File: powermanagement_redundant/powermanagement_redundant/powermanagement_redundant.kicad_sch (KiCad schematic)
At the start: 48 parts, among them J1 Screw_Terminal_01x01, J2 Screw_Terminal_01x01, J3 Screw_Terminal_01x01, J4 Screw_Terminal_01x01, J5 Screw_Terminal_01x01, J6 Screw_Terminal_01x01, J7 Screw_Terminal_01x01, J8 Screw_Terminal_01x01, SW1 SW_DIP_x01, SW2 SW_DIP_x01

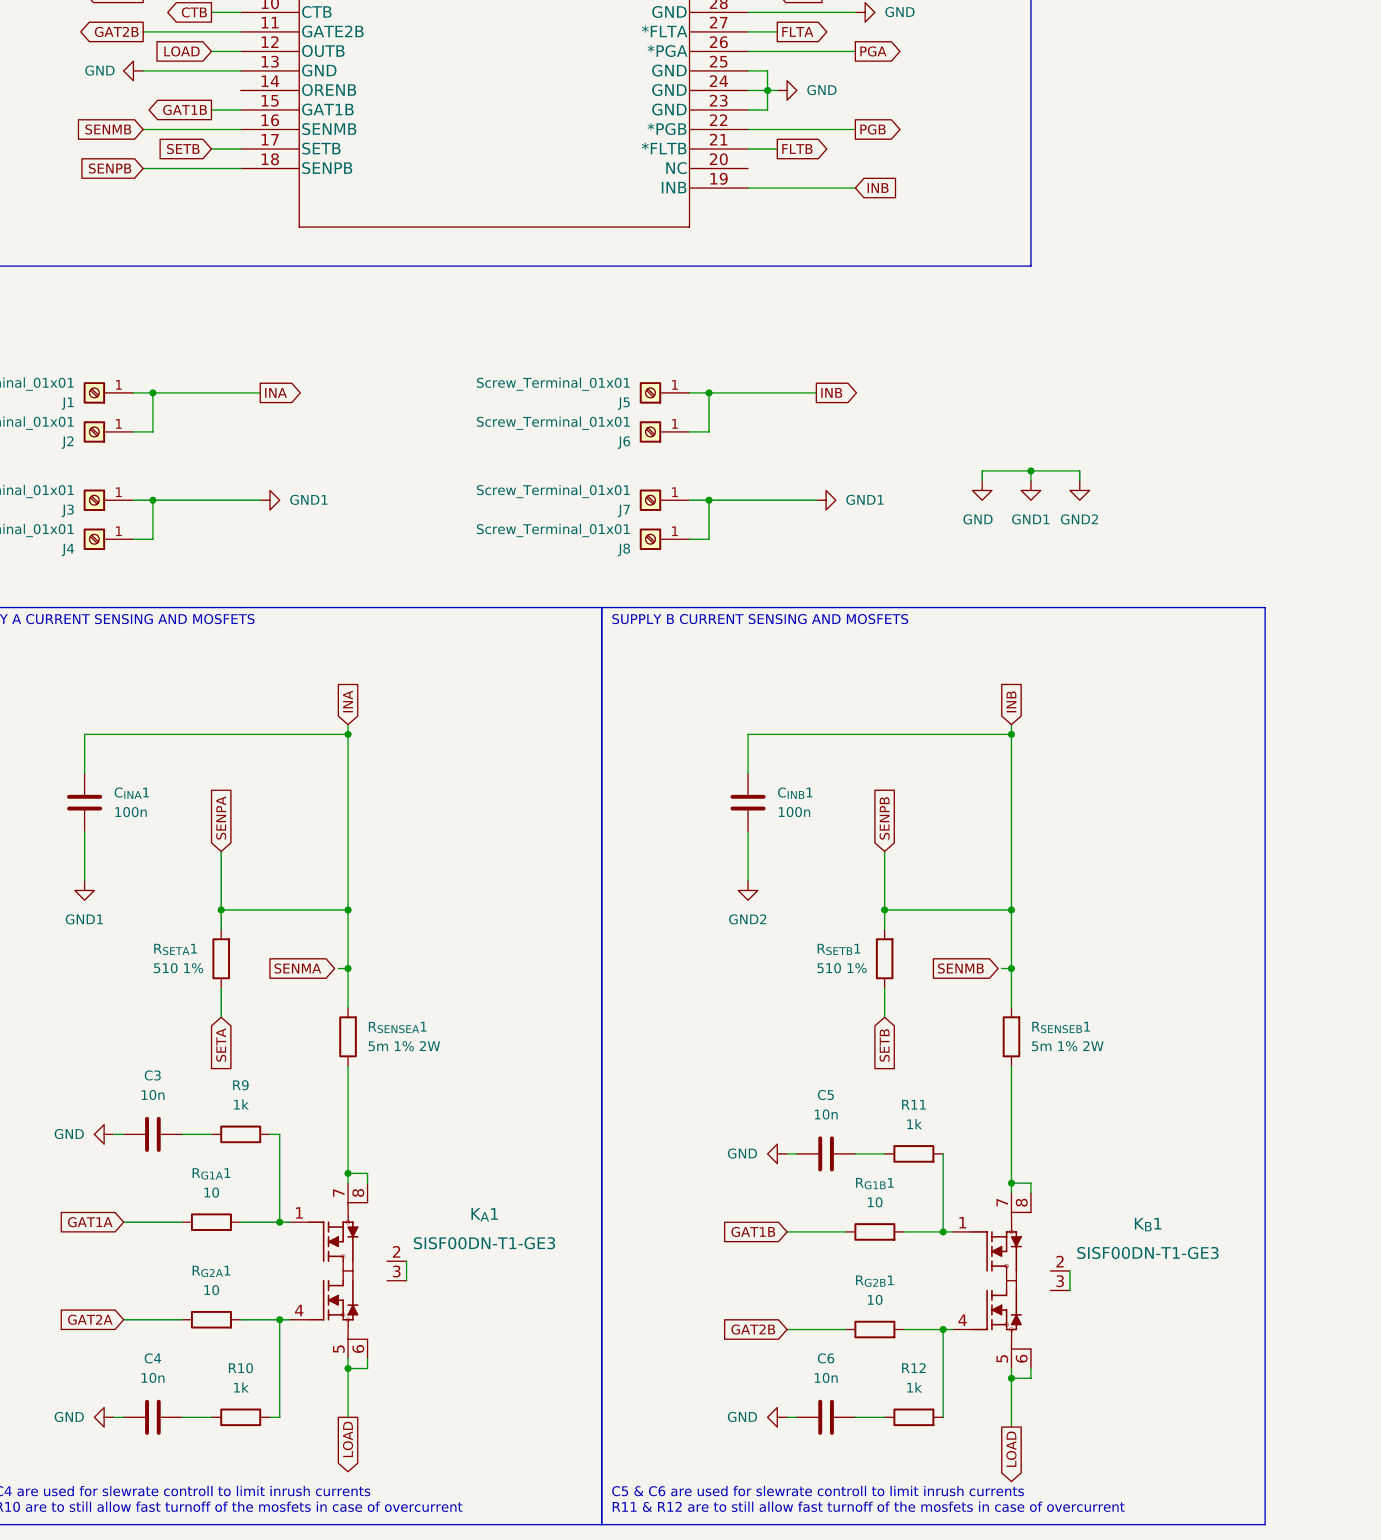
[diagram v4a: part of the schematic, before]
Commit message: Alle komponenten auf der Platine Platziert
Alles passt iwie ist aber knapp.
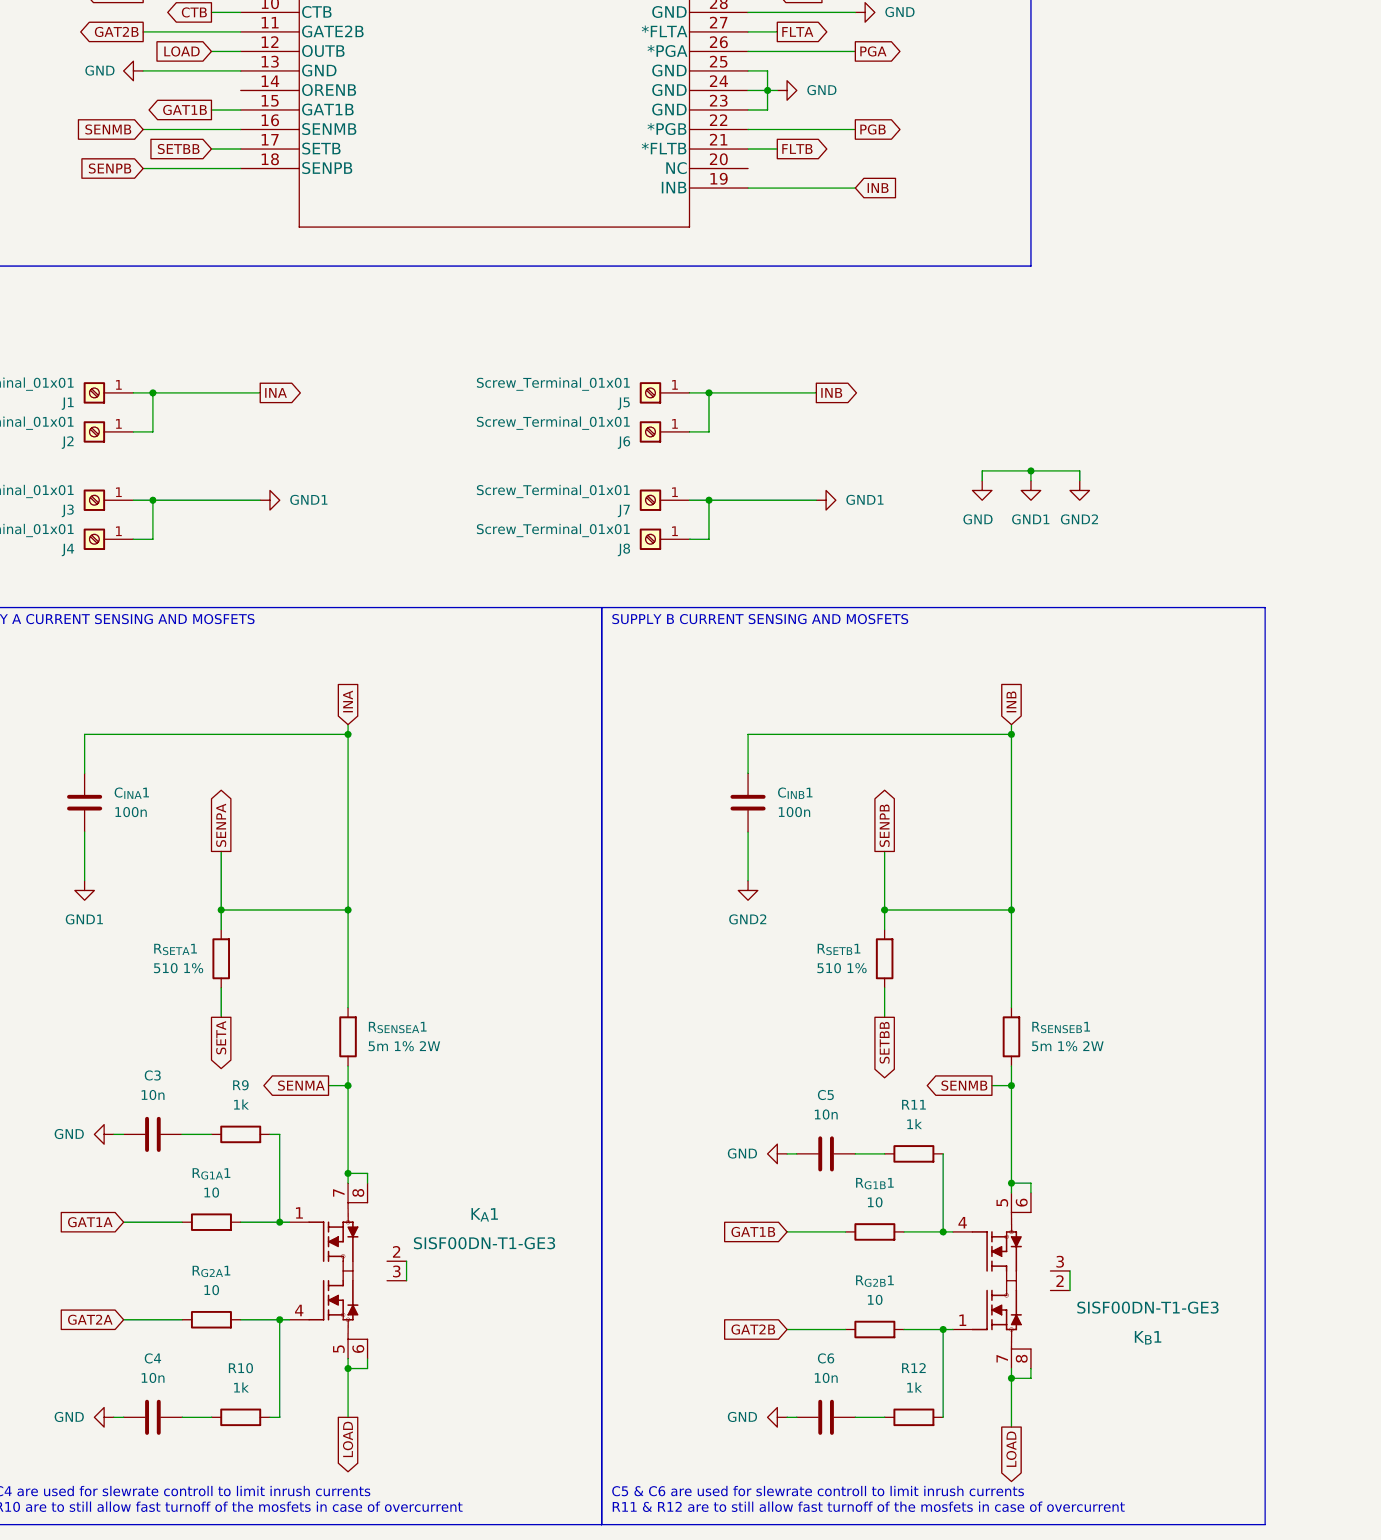
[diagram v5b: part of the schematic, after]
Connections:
- net LOAD: now also K_{B}1.7 (S1), K_{B}1.8 (S1); no longer K_{B}1.5 (S2), K_{B}1.6 (S2)
- net SENMA: now also K_{A}1.7 (S1), K_{A}1.8 (S1), R_{SENSEA}1.1
- net SENMB: now also K_{B}1.5 (S2), K_{B}1.6 (S2), R_{SENSEB}1.1
- net SETA: no longer A1.17 (SETB), R_{SETB}1.1
- net at R11.2, R_{G1B}1.2: now also K_{B}1.4 (G2); no longer K_{B}1.1 (G1)
- net at R12.2, R_{G2B}1.2: now also K_{B}1.1 (G1); no longer K_{B}1.4 (G2)
- new net SETBB: A1.17 (SETB), R_{SETB}1.1
